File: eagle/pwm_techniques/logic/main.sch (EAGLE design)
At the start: 42 parts, among them U1 LM2940T-10.0, U2 TLE2426ID, U3 LM358ADT

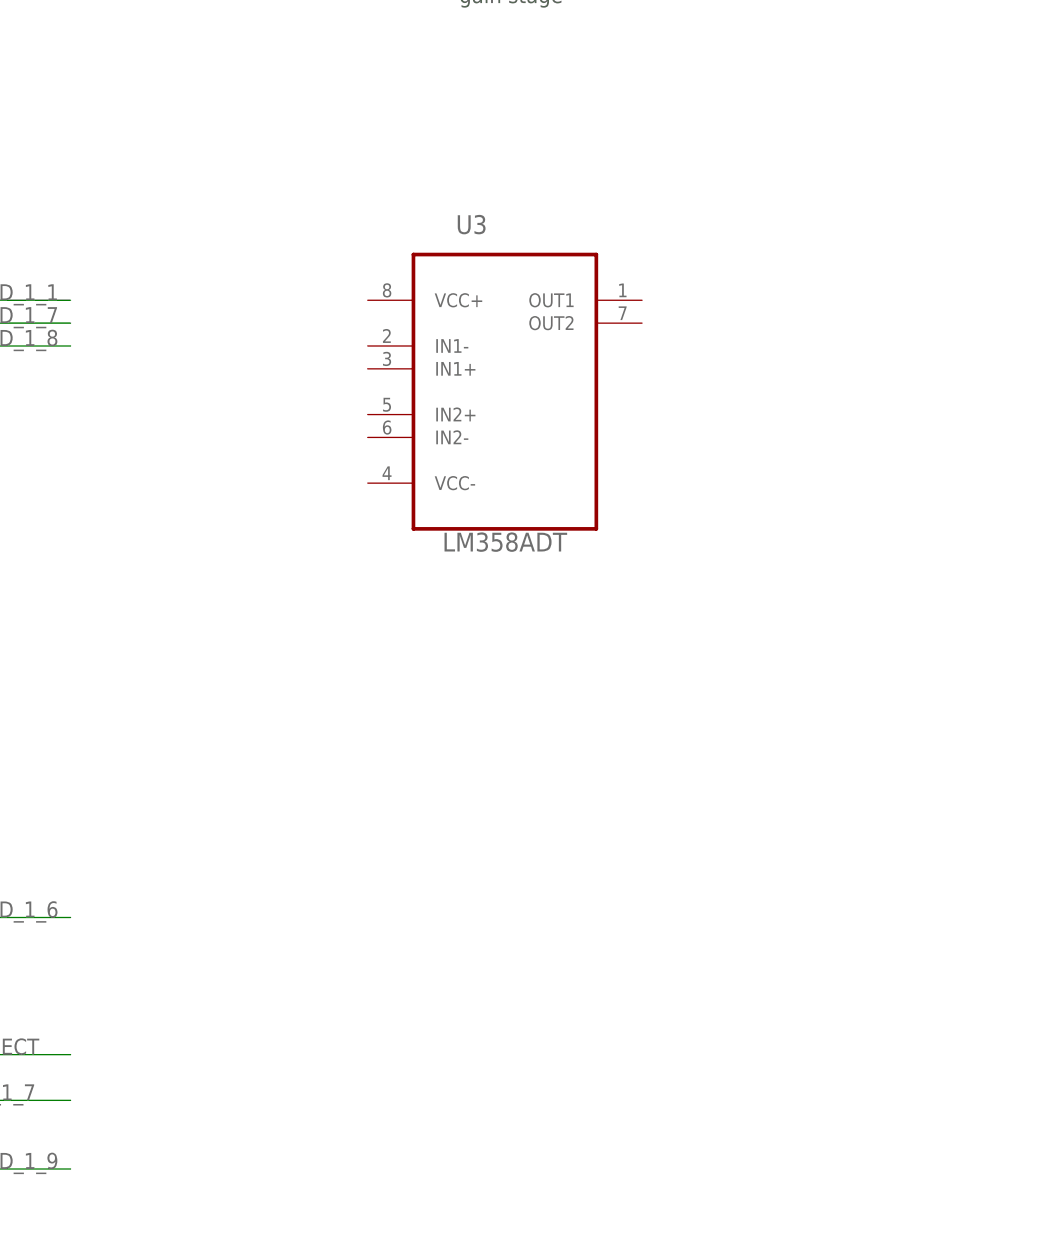
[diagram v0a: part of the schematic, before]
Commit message: [ update ] add gain stage
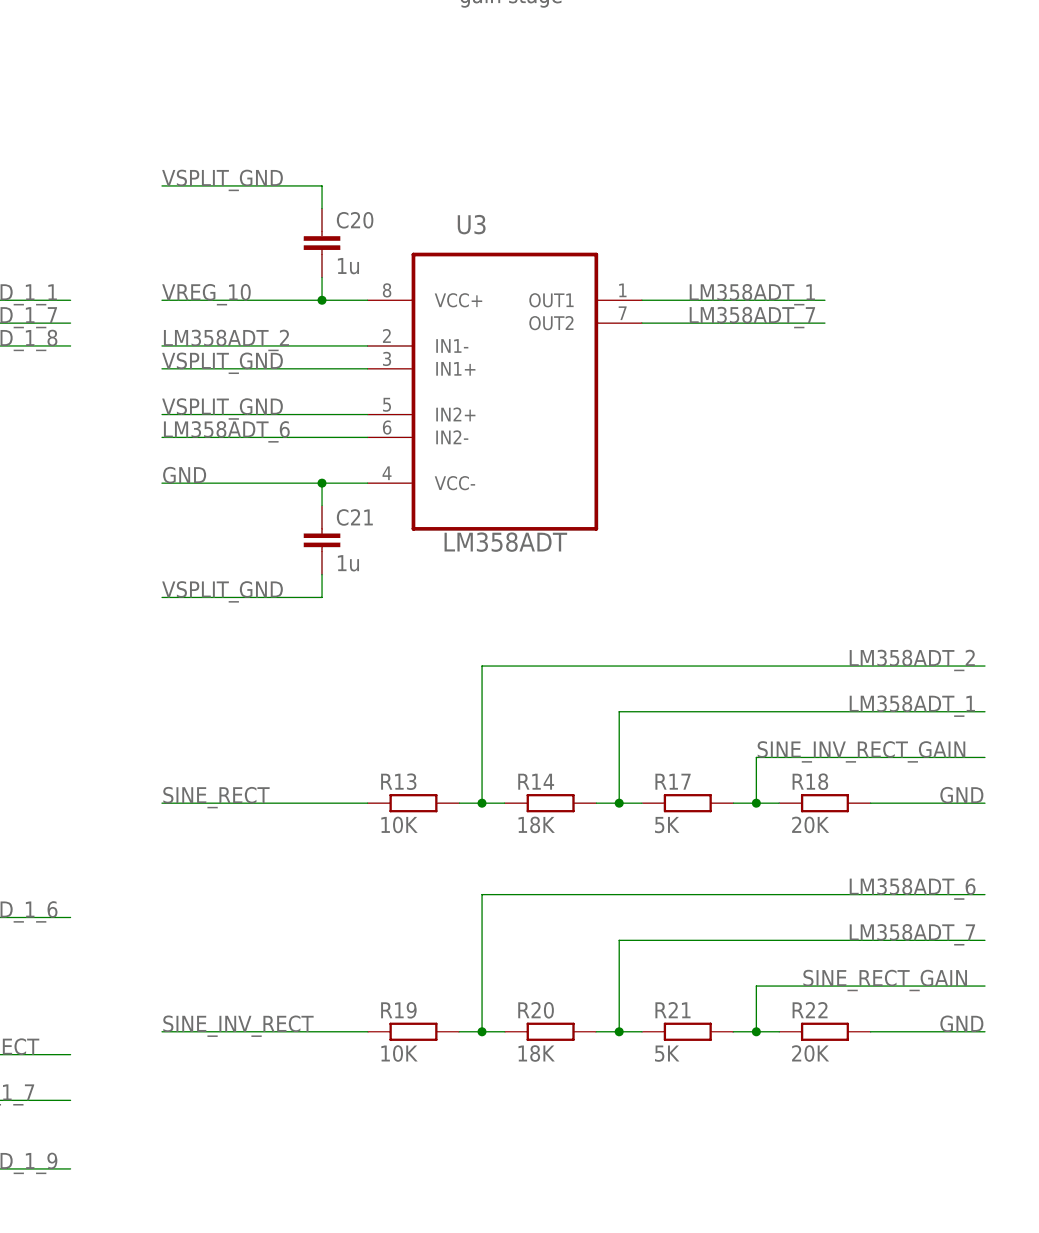
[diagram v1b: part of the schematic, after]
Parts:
- added C20, C21: 1u, rcl:C-EUC1206
- added R13, R19: 10K, resistor:R-EU_M1206
- added R14, R20: 18K, resistor:R-EU_M1206
- added R17, R21: 5K, resistor:R-EU_M1206
- added R18, R22: 20K, resistor:R-EU_M1206
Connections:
- new net LM358ADT_1: R14.2, R17.1, U3.OUT1
- new net LM358ADT_2: R13.2, R14.1, U3.IN1-
- new net LM358ADT_6: R19.2, R20.1, U3.IN2-
- new net LM358ADT_7: R20.2, R21.1, U3.OUT2
- new net SINE_INV_RECT_GAIN: R17.2, R18.1
- new net SINE_RECT_GAIN: R21.2, R22.1
- net GND: now also C21.1, R18.2, R22.2, U3.VCC-
- net SINE_INV_RECT: now also R19.1
- net SINE_RECT: now also R13.1
- net VREG_10: now also C20.2, U3.VCC+
- net VSPLIT_GND: now also C20.1, C21.2, U3.IN1+, U3.IN2+
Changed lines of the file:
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@@
 <part name="R16" library="resistor" deviceset="R-EU_" device="M1206" value="10K"/>
 <part name="U3" library="lm358ad" deviceset="LM358ADT" device=""/>
+<part name="C20" library="rcl" deviceset="C-EU" device="C1206" value="1u"/>
+<part name="C21" library="rcl" deviceset="C-EU" device="C1206" value="1u"/>
+<part name="R13" library="resistor" deviceset="R-EU_" device="M1206" value="10K"/>
+<part name="R14" library="resistor" deviceset="R-EU_" device="M1206" value="18K"/>
+<part name="R17" library="resistor" deviceset="R-EU_" device="M1206" value="5K"/>
+<part name="R18" library="resistor" deviceset="R-EU_" device="M1206" value="20K"/>
+<part name="R19" library="resistor" deviceset="R-EU_" device="M1206" value="10K"/>
+<part name="R20" library="resistor" deviceset="R-EU_" device="M1206" value="18K"/>
+<part name="R21" library="resistor" deviceset="R-EU_" device="M1206" value="5K"/>
+<part name="R22" library="resistor" deviceset="R-EU_" device="M1206" value="20K"/>
 </parts>
 <sheets>
@@
 <instance part="R16" gate="G$1" x="246.38" y="-35.56"/>
 <instance part="U3" gate="A" x="327.66" y="60.96"/>
+<instance part="C20" gate="G$1" x="307.34" y="76.2"/>
+<instance part="C21" gate="G$1" x="307.34" y="43.18"/>
+<instance part="R13" gate="G$1" x="317.5" y="12.7"/>
+<instance part="R14" gate="G$1" x="332.74" y="12.7"/>
+<instance part="R17" gate="G$1" x="347.98" y="12.7"/>
+<instance part="R18" gate="G$1" x="363.22" y="12.7"/>
+<instance part="R19" gate="G$1" x="317.5" y="-12.7"/>
+<instance part="R20" gate="G$1" x="332.74" y="-12.7"/>
+<instance part="R21" gate="G$1" x="347.98" y="-12.7"/>
+<instance part="R22" gate="G$1" x="363.22" y="-12.7"/>
 </instances>
 <busses>
@@
 <junction x="218.44" y="68.58"/>
 <pinref part="TL084ACD_1" gate="A" pin="VCC+"/>
+</segment>
+<segment>
+<wire x1="312.42" y1="68.58" x2="307.34" y2="68.58" width="0.1524" layer="91"/>
+<label x="289.56" y="68.58" size="1.778" layer="95"/>
+<pinref part="C20" gate="G$1" pin="2"/>
+<wire x1="307.34" y1="68.58" x2="289.56" y2="68.58" width="0.1524" layer="91"/>
+<wire x1="307.34" y1="68.58" x2="307.34" y2="71.12" width="0.1524" layer="91"/>
+<junction x="307.34" y="68.58"/>
+<pinref part="U3" gate="A" pin="VCC+"/>
 </segment>
 </net>
@@
 <pinref part="TL084ACD_1" gate="A" pin="VCC-"/>
 </segment>
+<segment>
+<wire x1="312.42" y1="48.26" x2="307.34" y2="48.26" width="0.1524" layer="91"/>
+<label x="289.56" y="48.26" size="1.778" layer="95"/>
+<pinref part="C21" gate="G$1" pin="1"/>
+<wire x1="307.34" y1="45.72" x2="307.34" y2="48.26" width="0.1524" layer="91"/>
+<wire x1="307.34" y1="48.26" x2="289.56" y2="48.26" width="0.1524" layer="91"/>
+<junction x="307.34" y="48.26"/>
+<pinref part="U3" gate="A" pin="VCC-"/>
+</segment>
+<segment>
+<pinref part="R18" gate="G$1" pin="2"/>
+<wire x1="368.3" y1="12.7" x2="381" y2="12.7" width="0.1524" layer="91"/>
+<label x="375.92" y="12.7" size="1.778" layer="95"/>
+</segment>
+<segment>
+<pinref part="R22" gate="G$1" pin="2"/>
+<wire x1="368.3" y1="-12.7" x2="381" y2="-12.7" width="0.1524" layer="91"/>
+<label x="375.92" y="-12.7" size="1.778" layer="95"/>
+</segment>
 </net>
 <net name="VSPLIT_GND" class="0">
@@
 <label x="200.66" y="58.42" size="1.778" layer="95"/>
 </segment>
+<segment>
+<pinref part="C20" gate="G$1" pin="1"/>
+<wire x1="307.34" y1="78.74" x2="307.34" y2="81.28" width="0.1524" layer="91"/>
+<wire x1="307.34" y1="81.28" x2="289.56" y2="81.28" width="0.1524" layer="91"/>
+<label x="289.56" y="81.28" size="1.778" layer="95"/>
+</segment>
+<segment>
+<pinref part="C21" gate="G$1" pin="2"/>
+<wire x1="307.34" y1="38.1" x2="307.34" y2="35.56" width="0.1524" layer="91"/>
+<wire x1="307.34" y1="35.56" x2="289.56" y2="35.56" width="0.1524" layer="91"/>
+<label x="289.56" y="35.56" size="1.778" layer="95"/>
+</segment>
+<segment>
+<pinref part="U3" gate="A" pin="IN1+"/>
+<wire x1="312.42" y1="60.96" x2="289.56" y2="60.96" width="0.1524" layer="91"/>
+<label x="289.56" y="60.96" size="1.778" layer="95"/>
+</segment>
+<segment>
+<pinref part="U3" gate="A" pin="IN2+"/>
+<wire x1="312.42" y1="55.88" x2="289.56" y2="55.88" width="0.1524" layer="91"/>
+<label x="289.56" y="55.88" size="1.778" layer="95"/>
+</segment>
 </net>
 <net name="N$2" class="0">
@@
 <junction x="256.54" y="-15.24"/>
 </segment>
+<segment>
+<pinref part="R19" gate="G$1" pin="1"/>
+<wire x1="312.42" y1="-12.7" x2="289.56" y2="-12.7" width="0.1524" layer="91"/>
+<label x="289.56" y="-12.7" size="1.778" layer="95"/>
+</segment>
 </net>
 <net name="SINE_RECT" class="0">
@@
 <junction x="256.54" y="-43.18"/>
 </segment>
-</net>
+<segment>
+<pinref part="R13" gate="G$1" pin="1"/>
+<wire x1="312.42" y1="12.7" x2="289.56" y2="12.7" width="0.1524" layer="91"/>
+<label x="289.56" y="12.7" size="1.778" layer="95"/>
+</segment>
+</net>
+<net name="LM358ADT_2" class="0">
+<segment>
+<pinref part="U3" gate="A" pin="IN1-"/>
+<wire x1="312.42" y1="63.5" x2="289.56" y2="63.5" width="0.1524" layer="91"/>
+<label x="289.56" y="63.5" size="1.778" layer="95"/>
+</segment>
+<segment>
+<pinref part="R13" gate="G$1" pin="2"/>
+<pinref part="R14" gate="G$1" pin="1"/>
+<wire x1="322.58" y1="12.7" x2="325.12" y2="12.7" width="0.1524" layer="91"/>
+<wire x1="325.12" y1="12.7" x2="327.66" y2="12.7" width="0.1524" layer="91"/>
+<wire x1="325.12" y1="12.7" x2="325.12" y2="27.94" width="0.1524" layer="91"/>
+<junction x="325.12" y="12.7"/>
+<wire x1="325.12" y1="27.94" x2="381" y2="27.94" width="0.1524" layer="91"/>
+<label x="365.76" y="27.94" size="1.778" layer="95"/>
+</segment>
+</net>
+<net name="LM358ADT_6" class="0">
+<segment>
+<pinref part="U3" gate="A" pin="IN2-"/>
+<wire x1="312.42" y1="53.34" x2="289.56" y2="53.34" width="0.1524" layer="91"/>
+<label x="289.56" y="53.34" size="1.778" layer="95"/>
+</segment>
+<segment>
+<pinref part="R19" gate="G$1" pin="2"/>
+<pinref part="R20" gate="G$1" pin="1"/>
+<wire x1="322.58" y1="-12.7" x2="325.12" y2="-12.7" width="0.1524" layer="91"/>
+<wire x1="325.12" y1="-12.7" x2="327.66" y2="-12.7" width="0.1524" layer="91"/>
+<wire x1="325.12" y1="-12.7" x2="325.12" y2="2.54" width="0.1524" layer="91"/>
+<junction x="325.12" y="-12.7"/>
+<wire x1="325.12" y1="2.54" x2="381" y2="2.54" width="0.1524" layer="91"/>
+<label x="365.76" y="2.54" size="1.778" layer="95"/>
+</segment>
+</net>
+<net name="LM358ADT_1" class="0">
+<segment>
+<pinref part="U3" gate="A" pin="OUT1"/>
+<wire x1="342.9" y1="68.58" x2="363.22" y2="68.58" width="0.1524" layer="91"/>
+<label x="347.98" y="68.58" size="1.778" layer="95"/>
+</segment>
+<segment>
+<pinref part="R14" gate="G$1" pin="2"/>
+<pinref part="R17" gate="G$1" pin="1"/>
+<wire x1="337.82" y1="12.7" x2="340.36" y2="12.7" width="0.1524" layer="91"/>
+<wire x1="340.36" y1="12.7" x2="342.9" y2="12.7" width="0.1524" layer="91"/>
+<wire x1="340.36" y1="12.7" x2="340.36" y2="22.86" width="0.1524" layer="91"/>
+<junction x="340.36" y="12.7"/>
+<wire x1="340.36" y1="22.86" x2="381" y2="22.86" width="0.1524" layer="91"/>
+<label x="365.76" y="22.86" size="1.778" layer="95"/>
+</segment>
+</net>
+<net name="LM358ADT_7" class="0">
+<segment>
+<pinref part="U3" gate="A" pin="OUT2"/>
+<wire x1="342.9" y1="66.04" x2="363.22" y2="66.04" width="0.1524" layer="91"/>
+<label x="347.98" y="66.04" size="1.778" layer="95"/>
+</segment>
+<segment>
+<pinref part="R20" gate="G$1" pin="2"/>
+<pinref part="R21" gate="G$1" pin="1"/>
+<wire x1="337.82" y1="-12.7" x2="340.36" y2="-12.7" width="0.1524" layer="91"/>
+<wire x1="340.36" y1="-12.7" x2="342.9" y2="-12.7" width="0.1524" layer="91"/>
+<wire x1="340.36" y1="-12.7" x2="340.36" y2="-2.54" width="0.1524" layer="91"/>
+<junction x="340.36" y="-12.7"/>
+<wire x1="340.36" y1="-2.54" x2="381" y2="-2.54" width="0.1524" layer="91"/>
+<label x="365.76" y="-2.54" size="1.778" layer="95"/>
+</segment>
+</net>
+<net name="SINE_INV_RECT_GAIN" class="0">
+<segment>
+<pinref part="R17" gate="G$1" pin="2"/>
+<pinref part="R18" gate="G$1" pin="1"/>
+<wire x1="353.06" y1="12.7" x2="355.6" y2="12.7" width="0.1524" layer="91"/>
+<wire x1="355.6" y1="12.7" x2="358.14" y2="12.7" width="0.1524" layer="91"/>
+<wire x1="355.6" y1="12.7" x2="355.6" y2="17.78" width="0.1524" layer="91"/>
+<junction x="355.6" y="12.7"/>
+<wire x1="355.6" y1="17.78" x2="381" y2="17.78" width="0.1524" layer="91"/>
+<label x="355.6" y="17.78" size="1.778" layer="95"/>
+</segment>
+</net>
+<net name="SINE_RECT_GAIN" class="0">
+<segment>
+<pinref part="R21" gate="G$1" pin="2"/>
+<pinref part="R22" gate="G$1" pin="1"/>
+<wire x1="353.06" y1="-12.7" x2="355.6" y2="-12.7" width="0.1524" layer="91"/>
+<wire x1="355.6" y1="-12.7" x2="358.14" y2="-12.7" width="0.1524" layer="91"/>
+<wire x1="355.6" y1="-12.7" x2="355.6" y2="-7.62" width="0.1524" layer="91"/>
+<junction x="355.6" y="-12.7"/>
+<wire x1="355.6" y1="-7.62" x2="381" y2="-7.62" width="0.1524" layer="91"/>
+<label x="360.68" y="-7.62" size="1.778" layer="95"/>
+</segment>
+</net>

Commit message: [ update ] pwm control stage, wip
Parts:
- added U4: TL494CD, tl494cd:TL494CD
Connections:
- new net TL494CD_0_3_10: U4.E2, U4.FEEDBACK
- net GND: now also U4.DTC, U4.GND
- net SINE_INV_RECT_GAIN: now also U4.1IN+
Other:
- note added: "pwm controller stage"
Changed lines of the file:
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@@
 <part name="R21" library="resistor" deviceset="R-EU_" device="M1206" value="5K"/>
 <part name="R22" library="resistor" deviceset="R-EU_" device="M1206" value="20K"/>
+<part name="U4" library="tl494cd" deviceset="TL494CD" device=""/>
 </parts>
 <sheets>
@@
 <text x="228.6" y="101.6" size="1.778" layer="97">sine rect generation stage</text>
 <text x="322.58" y="101.6" size="1.778" layer="97">gain stage</text>
+<text x="454.66" y="101.6" size="1.778" layer="97">pwm controller stage</text>
 </plain>
 <instances>
@@
 <instance part="R21" gate="G$1" x="347.98" y="-12.7"/>
 <instance part="R22" gate="G$1" x="363.22" y="-12.7"/>
+<instance part="U4" gate="A" x="464.82" y="55.88"/>
 </instances>
 <busses>
@@
 <label x="375.92" y="-12.7" size="1.778" layer="95"/>
 </segment>
+<segment>
+<pinref part="U4" gate="A" pin="GND"/>
+<wire x1="441.96" y1="33.02" x2="414.02" y2="33.02" width="0.1524" layer="91"/>
+<label x="414.02" y="33.02" size="1.778" layer="95"/>
+</segment>
+<segment>
+<pinref part="U4" gate="A" pin="DTC"/>
+<wire x1="441.96" y1="40.64" x2="414.02" y2="40.64" width="0.1524" layer="91"/>
+<label x="414.02" y="40.64" size="1.778" layer="95"/>
+</segment>
 </net>
 <net name="VSPLIT_GND" class="0">
@@
 <label x="355.6" y="17.78" size="1.778" layer="95"/>
 </segment>
+<segment>
+<pinref part="U4" gate="A" pin="1IN+"/>
+<wire x1="441.96" y1="63.5" x2="414.02" y2="63.5" width="0.1524" layer="91"/>
+<label x="414.02" y="63.5" size="1.778" layer="95"/>
+</segment>
 </net>
 <net name="SINE_RECT_GAIN" class="0">
@@
 </segment>
 </net>
+<net name="TL494CD_0_3_10" class="0">
+<segment>
+<wire x1="482.6" y1="7.62" x2="513.08" y2="7.62" width="0.1524" layer="91"/>
+<label x="482.6" y="7.62" size="1.778" layer="95"/>
+</segment>
+<segment>
+<wire x1="414.02" y1="38.1" x2="441.96" y2="38.1" width="0.1524" layer="91"/>
+<label x="414.02" y="38.1" size="1.778" layer="95"/>
+<pinref part="U4" gate="A" pin="FEEDBACK"/>
+</segment>
+<segment>
+<wire x1="487.68" y1="63.5" x2="515.62" y2="63.5" width="0.1524" layer="91"/>
+<label x="495.3" y="63.5" size="1.778" layer="95"/>
+<pinref part="U4" gate="A" pin="E2"/>
+</segment>
+</net>

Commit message: [ update ] logic schematics
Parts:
- removed C1, C3: 470n, rcl:C-EUC1206
- removed C2, C4: 22u, rcl:CPOL-EU085CS-1AR
- removed U1: LM2940T-10.0, lm2940t-10:LM2940T-10.0
- added C22, C24: 1u, rcl:C-EUC1206
- added C23, C25: 1n, rcl:C-EUC1206
- added C26, C28, C30, C32: 22u, rcl:CPOL-EU085CS-1AR
- added C27, C29, C31, C33: 470n, rcl:C-EUC1206
- added IC1, LM2940T_10: 7805T, linear:7805T
- added R23, R24, R26, R27: 1K, resistor:R-EU_M1206
- added R25, R28: 25K, resistor:R-EU_M1206
- added U5: SN74HC04D, sn74hc04d:SN74HC04D
- added U6: TL494CD, tl494cd:TL494CD
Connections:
- removed net TL494CD_0_3_10: U4.E2, U4.FEEDBACK
- new net N$4: U4.1IN-, U4.FEEDBACK
- new net N$5: C23.2, U4.CT
- new net N$6: R25.2, U4.RT
- new net N$7: U6.1IN-, U6.FEEDBACK
- new net N$8: C25.2, U6.CT
- new net N$9: R28.2, U6.RT
- new net PWM_CTL_HI_0: U5.1Y
- new net PWM_CTL_HI_1: U5.2Y
- new net PWM_CTL_LO_0: R23.2, R24.1, U4.C1, U4.C2, U5.1A
- new net PWM_CTL_LO_1: R26.2, R27.1, U5.2A, U6.C1, U6.C2
- new net VREG_5: C28.+, C29.1, IC1.VO, U5.VCC
- net GND: now also C22.1, C23.1, C24.1, C25.1, C26.-, C27.2, C28.-, C29.2, C30.-, C31.2, C32.-, C33.2, IC1.GND, LM2940T_10.GND, R24.2, R25.1, R27.2, R28.1, U4.E1, U4.E2, U4.OUTPUT_CTRL, U5.GND, U6.DTC, U6.E1, U6.E2, U6.GND, U6.OUTPUT_CTRL; no longer C1.2, C2.-, C3.2, C4.-, U1.GND
- net SINE_RECT_GAIN: now also U6.1IN+
- net VBAT_12: now also C26.+, C27.1, C30.+, C31.1, IC1.VI, LM2940T_10.VI; no longer C1.1, C4.+, U1.IN
- net VREG_10: now also C22.2, C24.2, C32.+, C33.1, LM2940T_10.VO, R23.1, R26.1, U4.VCC, U6.VCC; no longer C2.+, C3.1, U1.OUT
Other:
- note added: "WARNING: actually a LM2940T, 7805T used only for footprint"
- note added: "half wave generation stage"
- note removed: "sine rect generation stage"
- moved on the sheet: C10, C6, C7, C8, C9, U2
